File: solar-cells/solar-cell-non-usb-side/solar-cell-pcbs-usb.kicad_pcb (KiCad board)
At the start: 2 copper layers, 80 x 103.5 mm, 13 parts, among them J1 Solar Cell

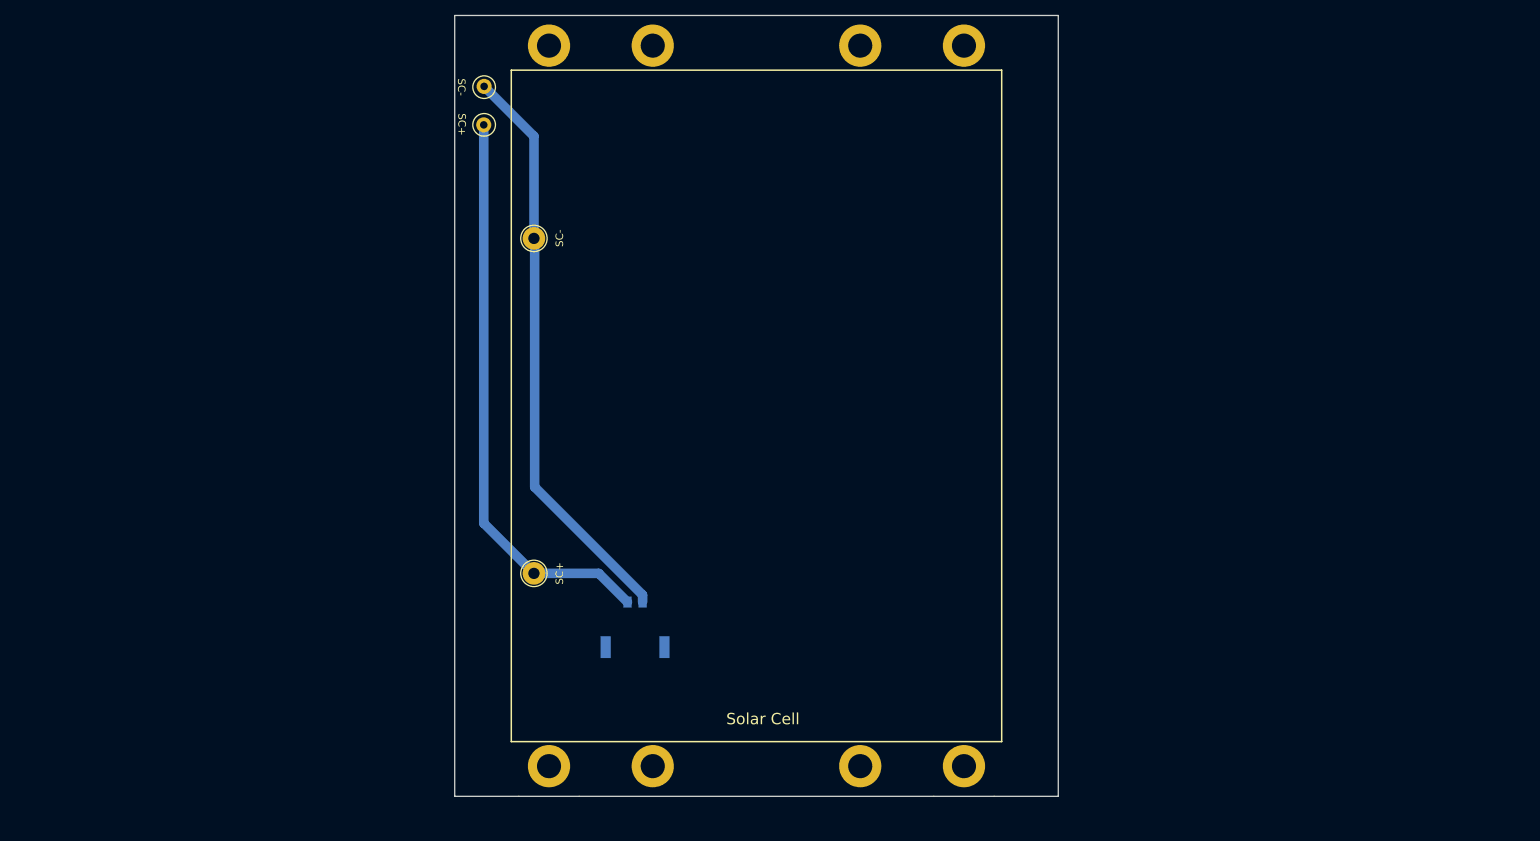
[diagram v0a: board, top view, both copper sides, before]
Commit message: updated schematic for new solar cells
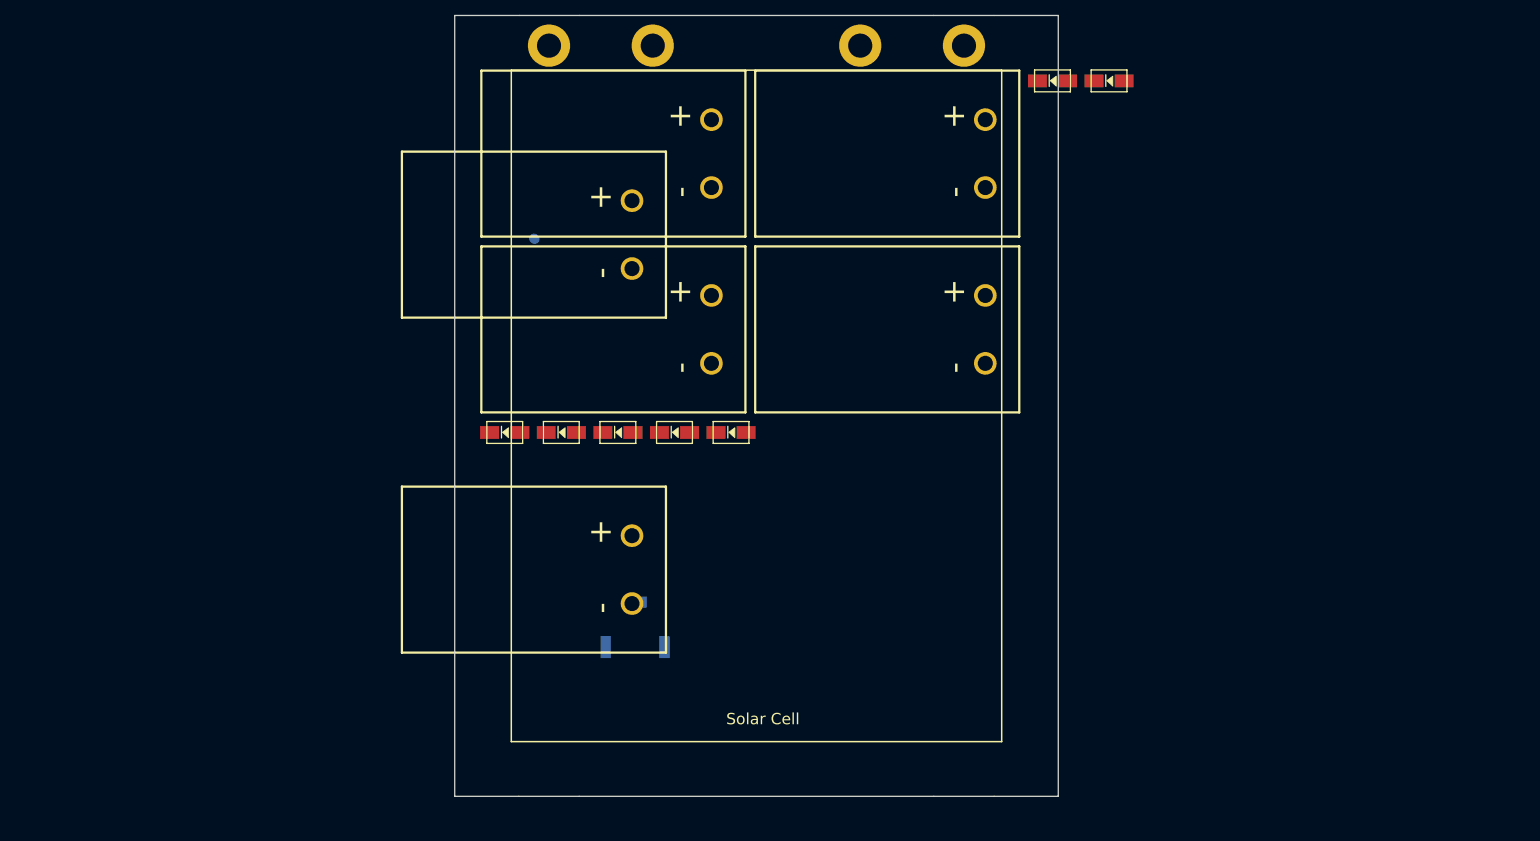
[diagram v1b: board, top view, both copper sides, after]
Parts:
- removed H5, H6, H7, H8: MountingHole, MountingHole:MountingHole_3.2mm_M3_DIN965_Pad
- removed TP1: SC+, TestPoint:TestPoint_Loop_D1.80mm_Drill1.0mm_Beaded
- removed TP2: SC-, TestPoint:TestPoint_Loop_D1.80mm_Drill1.0mm_Beaded
- added D1: CDBA240LL-HF, ISP:DO-214AC, F.Cu at (78.7, 94.0)
- added D2: CDBA240LL-HF, ISP:DO-214AC, F.Cu at (101.2, 94.0)
- added D3: CDBA240LL-HF, ISP:DO-214AC, F.Cu at (108.7, 94.0)
- added D4: CDBA240LL-HF, ISP:DO-214AC, F.Cu at (151.3, 47.4)
- added D5: CDBA240LL-HF, ISP:DO-214AC, F.Cu at (86.2, 94.0)
- added D6: CDBA240LL-HF, ISP:DO-214AC, F.Cu at (93.7, 94.0)
- added D9: CDBA240LL-HF, ISP:DO-214AC, F.Cu at (158.8, 47.4)
- added SC3: SM101K07TF, ISP:SM101K07TF, F.Cu at (129.4, 80.9)
- added SC4: SM101K07TF, ISP:SM101K07TF, F.Cu at (129.4, 57.6)
- added SC5: SM101K07TF, ISP:SM101K07TF, F.Cu at (93.1, 80.9)
- added SC6: SM101K07TF, ISP:SM101K07TF, F.Cu at (93.1, 57.6)
- H1, H2, H3, H4: value MountingHole -> MountingHole_Pad
- SC1: value SC+ -> SM101K07TF; footprint TestPoint:TestPoint_THTPad_D3.0mm_Drill1.5mm -> ISP:SM101K07TF
- SC2: value SC- -> SM101K07TF; footprint TestPoint:TestPoint_THTPad_D3.0mm_Drill1.5mm -> ISP:SM101K07TF
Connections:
- H1 pad 1: (no net) -> GND
- H2 pad 1: (no net) -> GND
- H3 pad 1: (no net) -> GND
- H4 pad 1: (no net) -> GND
- J1 pad 2: SC+ -> VSOLAR
- SC1 pad 1: SC+ -> Net-(D1-Pad1)
- SC2 pad 1: GND -> Net-(D1-Pad2)
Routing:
- net GND: track 77.0 -> 0.00 mm
- net SC+: track 76.2 -> 0.00 mm

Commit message: hole positioning
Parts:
- added H5: MountingHole_Pad, MountingHole:MountingHole_3.2mm_M3_DIN965_Pad, F.Cu at (84.6, 138.2)
- added H6: MountingHole_Pad, MountingHole:MountingHole_3.2mm_M3_DIN965_Pad, F.Cu at (98.3, 138.2)
- added H7: MountingHole_Pad, MountingHole:MountingHole_3.2mm_M3_DIN965_Pad, F.Cu at (128.2, 138.2)
- added H8: MountingHole_Pad, MountingHole:MountingHole_3.2mm_M3_DIN965_Pad, F.Cu at (139.6, 138.2)
- moved D9 100.2 mm to (59.1, 57.2)
- moved SC6 99.7 mm to (188.1, 88.1)
- moved D3 90.3 mm to (29.5, 137.3)
- moved D2 79.3 mm to (39.4, 143.7)
- moved SC3 68.3 mm to (188.8, 114.7)
- moved SC5 67.4 mm to (31.5, 53.6)
- moved SC4 61.0 mm to (190.1, 64.3)
- moved D4 59.4 mm to (210.7, 46.5)
- moved D6 58.3 mm to (64.7, 144.6)
- moved D1 53.3 mm to (52.9, 140.6)
- moved SC2 47.7 mm to (37.6, 84.1)
- moved SC1 47.0 mm to (35.9, 118.0)
- moved D5 45.0 mm to (61.9, 131.9)
- moved J1 36.4 mm to (62.2, 106.1)
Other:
- board text removed: "+"
- board text removed: "-"
- board text removed: "Solar Cell"
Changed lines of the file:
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@@
   (net 7 "Net-(D5-Pad2)")
   (net 8 "VSOLAR")
-  (footprint "ISP:DO-214AC" (layer "F.Cu")
-    (at 93.73 94.02)
+  (footprint "MountingHole:MountingHole_3.2mm_M3_DIN965_Pad" (layer "F.Cu")
+    (at 128.25 138.25)
+    (descr "Mounting Hole 3.2mm, M3, DIN965")
+    (tags "mounting hole 3.2mm m3 din965")
+    (property "Sheetfile" "solar-cell-pcbs-usb.kicad_sch")
+    (property "Sheetname" "")
+    (attr exclude_from_pos_files)
+    (fp_text reference "H7" (at 0 -3.8) (layer "F.SilkS")
+      (effects (font (size 1 1) (thickness 0.15)))
+    )
+    (fp_text value "MountingHole_Pad" (at 0 3.8) (layer "F.Fab")
+      (effects (font (size 1 1) (thickness 0.15)))
+    )
+    (fp_text user "${REFERENCE}" (at 0 0) (layer "F.Fab")
+      (effects (font (size 1 1) (thickness 0.15)))
+    )
+    (fp_circle (center 0 0) (end 2.8 0) (layer "Cmts.User") (width 0.15) (fill none))
+    (fp_circle (center 0 0) (end 3.05 0) (layer "F.CrtYd") (width 0.05) (fill none))
+    (pad "1" thru_hole circle (at 0 0) (size 5.6 5.6) (drill 3.2) (layers *.Cu *.Mask)
+      (net 1 "GND") (pinfunction "1") (pintype "input"))
+  )
+  (footprint "ISP:DO-214AC" (layer "F.Cu")
+    (at 64.69 144.6)
     (property "Sheetfile" "solar-cell-pcbs-usb.kicad_sch")
     (property "Sheetname" "")
@@
   )
   (footprint "ISP:SM101K07TF" (layer "F.Cu")
-    (at 82.6 112.7)
+    (at 35.9 118.04)
     (property "Sheetfile" "solar-cell-pcbs-usb.kicad_sch")
     (property "Sheetname" "")
@@
   )
   (footprint "ISP:SM101K07TF" (layer "F.Cu")
-    (at 129.43 80.86)
+    (at 188.78 114.66)
     (property "Sheetfile" "solar-cell-pcbs-usb.kicad_sch")
     (property "Sheetname" "")
@@
   )
   (footprint "ISP:DO-214AC" (layer "F.Cu")
-    (at 158.83 47.42)
+    (at 59.12 57.17)
     (property "Sheetfile" "solar-cell-pcbs-usb.kicad_sch")
     (property "Sheetname" "")
@@
   )
   (footprint "ISP:DO-214AC" (layer "F.Cu")
-    (at 101.23 94.02)
+    (at 39.41 143.68)
     (property "Sheetfile" "solar-cell-pcbs-usb.kicad_sch")
     (property "Sheetname" "")
@@
       (net 4 "Net-(D2-Pad2)") (pinfunction "A") (pintype "passive"))
   )
+  (footprint "MountingHole:MountingHole_3.2mm_M3_DIN965_Pad" (layer "F.Cu")
+    (at 139.6 138.25)
+    (descr "Mounting Hole 3.2mm, M3, DIN965")
+    (tags "mounting hole 3.2mm m3 din965")
+    (property "Sheetfile" "solar-cell-pcbs-usb.kicad_sch")
+    (property "Sheetname" "")
+    (attr exclude_from_pos_files)
+    (fp_text reference "H8" (at 0 -3.8) (layer "F.SilkS")
+      (effects (font (size 1 1) (thickness 0.15)))
+    )
+    (fp_text value "MountingHole_Pad" (at 0 3.8) (layer "F.Fab")
+      (effects (font (size 1 1) (thickness 0.15)))
+    )
+    (fp_text user "${REFERENCE}" (at 0 0) (layer "F.Fab")
+      (effects (font (size 1 1) (thickness 0.15)))
+    )
+    (fp_circle (center 0 0) (end 2.8 0) (layer "Cmts.User") (width 0.15) (fill none))
+    (fp_circle (center 0 0) (end 3.05 0) (layer "F.CrtYd") (width 0.05) (fill none))
+    (pad "1" thru_hole circle (at 0 0) (size 5.6 5.6) (drill 3.2) (layers *.Cu *.Mask)
+      (net 1 "GND") (pinfunction "1") (pintype "input"))
+  )
   (footprint "ISP:SM101K07TF" (layer "F.Cu")
-    (at 93.13 80.86)
+    (at 31.48 53.57)
     (property "Sheetfile" "solar-cell-pcbs-usb.kicad_sch")
     (property "Sheetname" "")
@@
   )
   (footprint "ISP:DO-214AC" (layer "F.Cu")
-    (at 108.73 94.02)
+    (at 29.51 137.33)
     (property "Sheetfile" "solar-cell-pcbs-usb.kicad_sch")
     (property "Sheetname" "")
@@
   )
   (footprint "ISP:SM101K07TF" (layer "F.Cu")
-    (at 82.6 68.3)
+    (at 37.6 84.07)
     (property "Sheetfile" "solar-cell-pcbs-usb.kicad_sch")
     (property "Sheetname" "")
@@
   )
   (footprint "ISP:DO-214AC" (layer "F.Cu")
-    (at 78.73 94.02)
+    (at 52.9 140.63)
     (property "Sheetfile" "solar-cell-pcbs-usb.kicad_sch")
     (property "Sheetname" "")
@@
   )
   (footprint "ISP:DO-214AC" (layer "F.Cu")
-    (at 86.23 94.02)
+    (at 61.9 131.9)
     (property "Sheetfile" "solar-cell-pcbs-usb.kicad_sch")
     (property "Sheetname" "")
@@
       (net 7 "Net-(D5-Pad2)") (pinfunction "A") (pintype "passive"))
   )
+  (footprint "MountingHole:MountingHole_3.2mm_M3_DIN965_Pad" (layer "F.Cu")
+    (at 84.6 138.25)
+    (descr "Mounting Hole 3.2mm, M3, DIN965")
+    (tags "mounting hole 3.2mm m3 din965")
+    (property "Sheetfile" "solar-cell-pcbs-usb.kicad_sch")
+    (property "Sheetname" "")
+    (attr exclude_from_pos_files)
+    (fp_text reference "H5" (at 0 -3.8) (layer "F.SilkS")
+      (effects (font (size 1 1) (thickness 0.15)))
+    )
+    (fp_text value "MountingHole_Pad" (at 0 3.8) (layer "F.Fab")
+      (effects (font (size 1 1) (thickness 0.15)))
+    )
+    (fp_text user "${REFERENCE}" (at 0 0) (layer "F.Fab")
+      (effects (font (size 1 1) (thickness 0.15)))
+    )
+    (fp_circle (center 0 0) (end 2.8 0) (layer "Cmts.User") (width 0.15) (fill none))
+    (fp_circle (center 0 0) (end 3.05 0) (layer "F.CrtYd") (width 0.05) (fill none))
+    (pad "1" thru_hole circle (at 0 0) (size 5.6 5.6) (drill 3.2) (layers *.Cu *.Mask)
+      (net 1 "GND") (pinfunction "1") (pintype "input"))
+  )
   (footprint "ISP:SM101K07TF" (layer "F.Cu")
-    (at 129.43 57.56)
+    (at 190.07 64.28)
     (property "Sheetfile" "solar-cell-pcbs-usb.kicad_sch")
     (property "Sheetname" "")
@@
   )
   (footprint "ISP:DO-214AC" (layer "F.Cu")
-    (at 151.33 47.42)
+    (at 210.7 46.46)
     (property "Sheetfile" "solar-cell-pcbs-usb.kicad_sch")
     (property "Sheetname" "")
@@
       (net 1 "GND") (pinfunction "1") (pintype "input"))
   )
+  (footprint "MountingHole:MountingHole_3.2mm_M3_DIN965_Pad" (layer "F.Cu")
+    (at 98.35 138.25)
+    (descr "Mounting Hole 3.2mm, M3, DIN965")
+    (tags "mounting hole 3.2mm m3 din965")
+    (property "Sheetfile" "solar-cell-pcbs-usb.kicad_sch")
+    (property "Sheetname" "")
+    (attr exclude_from_pos_files)
+    (fp_text reference "H6" (at 0 -3.8) (layer "F.SilkS")
+      (effects (font (size 1 1) (thickness 0.15)))
+    )
+    (fp_text value "MountingHole_Pad" (at 0 3.8) (layer "F.Fab")
+      (effects (font (size 1 1) (thickness 0.15)))
+    )
+    (fp_text user "${REFERENCE}" (at 0 0) (layer "F.Fab")
+      (effects (font (size 1 1) (thickness 0.15)))
+    )
+    (fp_circle (center 0 0) (end 2.8 0) (layer "Cmts.User") (width 0.15) (fill none))
+    (fp_circle (center 0 0) (end 3.05 0) (layer "F.CrtYd") (width 0.05) (fill none))
+    (pad "1" thru_hole circle (at 0 0) (size 5.6 5.6) (drill 3.2) (layers *.Cu *.Mask)
+      (net 1 "GND") (pinfunction "1") (pintype "input"))
+  )
   (footprint "ISP:SM101K07TF" (layer "F.Cu")
-    (at 93.13 57.56)
+    (at 188.08 88.09)
     (property "Sheetfile" "solar-cell-pcbs-usb.kicad_sch")
     (property "Sheetname" "")
@@
   )
   (footprint "Molex_PicoLock_2p_2mm_2053380002:2053380002" (layer "B.Cu")
-    (at 97 116.5)
+    (at 62.16 106.11)
     (property "Sheetfile" "solar-cell-pcbs-usb.kicad_sch")
     (property "Sheetname" "")
     (attr through_hole)
-    (fp_text reference "J1" (at -1.0285 -4.950001 180) (layer "B.SilkS")
+    (fp_text reference "J1" (at -1.0285 -4.950001) (layer "B.SilkS")
       (effects (font (size 1 1) (thickness 0.15)) (justify mirror))
     )
-    (fp_text value "Solar Cell" (at -0.9535 9.874999 180) (layer "B.SilkS")
+    (fp_text value "Solar Cell" (at -0.9535 9.874999) (layer "B.SilkS")
       (effects (font (size 1 1) (thickness 0.15)) (justify mirror))
     )
-    (fp_text user "Copyright 2021 Accelerated Designs. All rights reserved." (at 0 0 180) (layer "Cmts.User")
+    (fp_text user "Copyright 2021 Accelerated Designs. All rights reserved." (at 0 0) (layer "Cmts.User")
       (effects (font (size 0.127 0.127) (thickness 0.002)))
     )
-    (fp_text user "*" (at 0 0 180) (layer "B.Fab")
+    (fp_text user "*" (at 0 0) (layer "B.Fab")
       (effects (font (size 1 1) (thickness 0.15)) (justify mirror))
     )
@@
     (pad "4" smd rect (at -4.894997 5.974999) (size 1.35 2.899999) (layers "B.Cu" "B.Paste" "B.Mask"))
   )
-  (gr_line (start 79.6 46) (end 144.6 46) (layer "F.SilkS") (width 0.2))
-  (gr_line (start 79.6 135) (end 144.6 135) (layer "F.SilkS") (width 0.2))
-  (gr_line (start 79.6 135) (end 79.6 46) (layer "F.SilkS") (width 0.2))
-  (gr_line (start 144.6 46) (end 144.6 135) (layer "F.SilkS") (width 0.2))
   (gr_line (start 143.6 38.75) (end 152.1 38.75) (layer "Edge.Cuts") (width 0.1))
   (gr_line (start 80.6 142.25) (end 88.6 142.25) (layer "Edge.Cuts") (width 0.1))
@@
   (gr_line (start 80.65 38.75) (end 72.1 38.75) (layer "Edge.Cuts") (width 0.1))
   (gr_line (start 72.1 142.25) (end 72.1 38.75) (layer "Edge.Cuts") (width 0.1))
-  (gr_text "-" (at 97 113.65 -180) (layer "B.SilkS")
-    (effects (font (size 1.5 1.5) (thickness 0.3)) (justify mirror))
-  )
-  (gr_text "+" (at 95.025 113.425) (layer "B.SilkS")
-    (effects (font (size 1.5 1.5) (thickness 0.3)) (justify mirror))
-  )
-  (gr_text "Solar Cell" (at 112.95 132) (layer "F.SilkS")
-    (effects (font (size 1.5 1.5) (thickness 0.3)))
-  )
   (dimension (type aligned) (layer "Dwgs.User")
     (pts (xy 98.35 138.25) (xy 98.25 124.025))
